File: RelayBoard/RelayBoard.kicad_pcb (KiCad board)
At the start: 2 copper layers, 49.5 x 49.5 mm, 17 parts, among them K1 CONN_3, K2 CONN_3, K3 CONN_3, Q1 2N4401, Q2 2N4401, Q3 2N4401

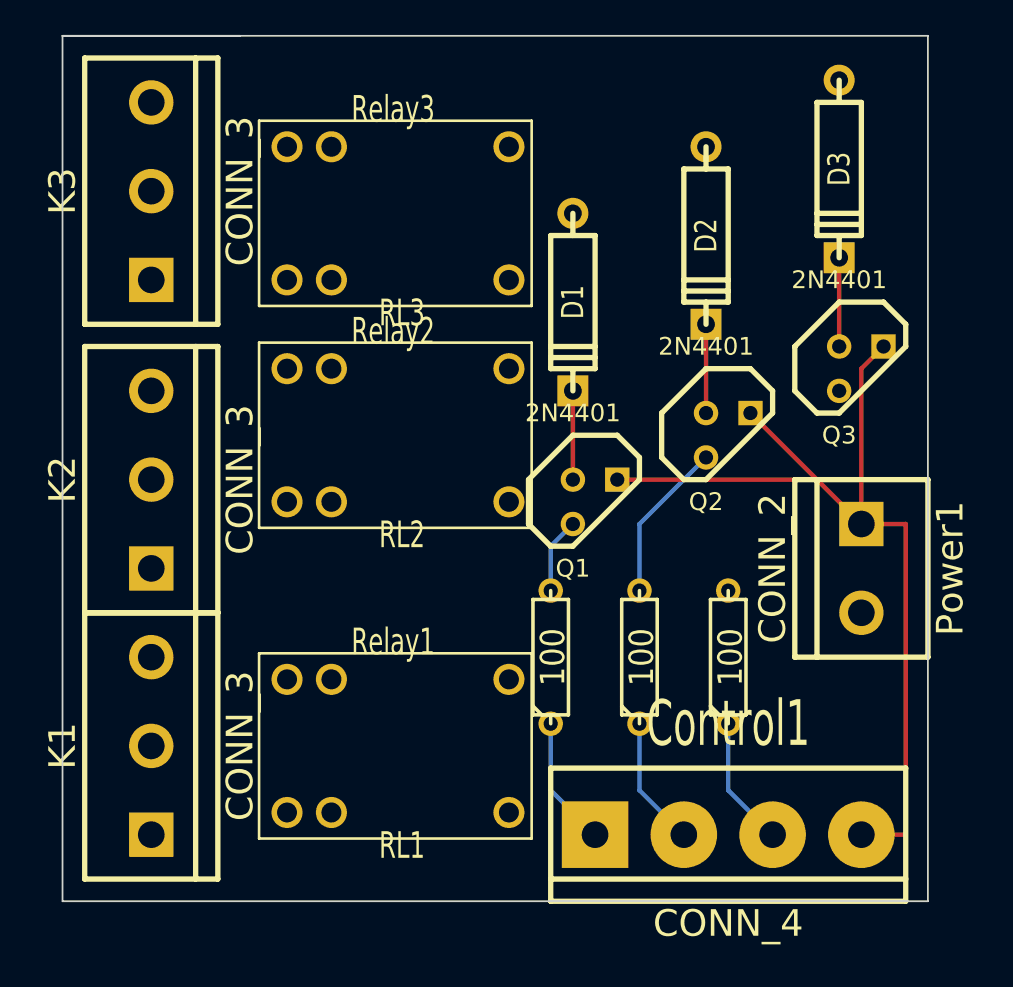
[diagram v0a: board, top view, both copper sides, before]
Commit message: Completed RelayBoard PCB Design
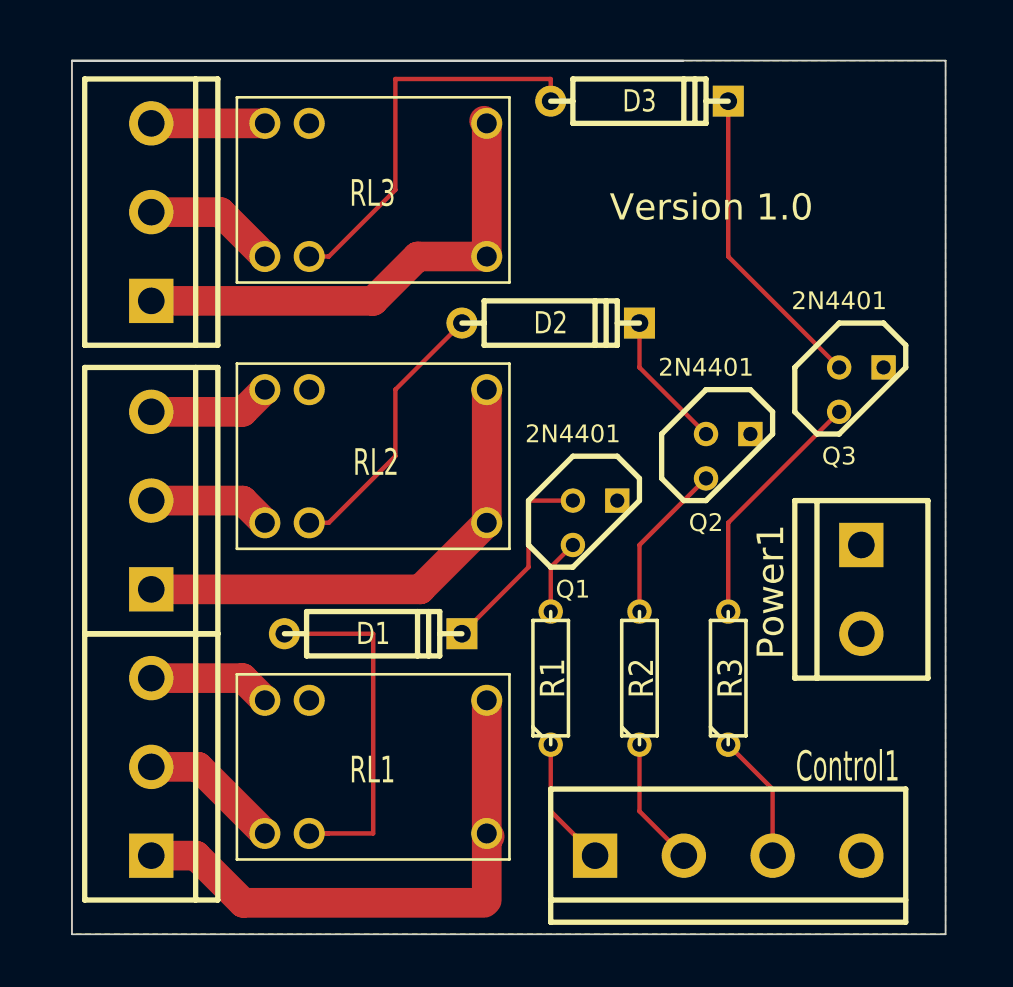
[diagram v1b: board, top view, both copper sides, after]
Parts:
- R1: value 100 -> R1
- R2: value 100 -> R2
- R3: value 100 -> R3
- moved D1 22.2 mm to (142.2, 102.8), turned to 0 degrees
- moved D3 12.1 mm to (157.5, 72.3), turned to 0 degrees
- moved D2 10.2 mm to (152.4, 85.0), turned to 0 degrees
- moved RL3 1.85 mm to (142.2, 77.4)
- moved RL1 1.75 mm to (142.2, 110.4)
- moved RL2 1.75 mm to (142.2, 92.6)
- moved Control1 1.20 mm to (162.6, 115.5)
- moved K1 1.20 mm to (129.5, 110.4)
- moved K2 1.20 mm to (129.5, 95.2)
- moved K3 1.20 mm to (129.5, 78.7)
- moved Power1 1.20 mm to (170.2, 100.3)
- moved Q1 1.20 mm to (154.9, 96.5)
- moved Q2 1.20 mm to (162.6, 92.6)
- moved Q3 1.20 mm to (170.2, 88.8)
- moved R1 1.20 mm to (152.4, 105.3)
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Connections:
- K1 pad 1: N-000005 -> N-000009
- K1 pad 2: N-000004 -> N-000007
- K1 pad 3: N-000003 -> N-000008
- K2 pad 1: N-000009 -> N-000002
- K2 pad 2: N-000007 -> N-000006
- K2 pad 3: N-000008 -> N-000001
- K3 pad 1: N-000002 -> N-000005
- K3 pad 2: N-000006 -> N-000004
- K3 pad 3: N-000001 -> N-000003
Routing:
- net GND: track 54.0 -> 0.00 mm
- net N-000009: track 0.00 -> 31.9 mm
- net N-000002: track 0.00 -> 28.4 mm
- net N-000005: track 0.00 -> 28.1 mm
- net N-0000020: track 0.00 -> 23.0 mm
- net N-0000022: track 0.00 -> 21.3 mm
- net N-0000021: track 0.00 -> 15.7 mm
- net N-0000015: track 0.00 -> 14.1 mm
- net N-0000010: track 5.08 -> 17.9 mm
- net N-000007: track 0.00 -> 8.08 mm
- net N-000004: track 0.00 -> 7.55 mm
- net N-000008: track 0.00 -> 7.03 mm
- net N-000006: track 0.00 -> 7.03 mm
- net N-000001: track 0.00 -> 7.03 mm
- net N-0000014: track 5.08 -> 11.7 mm
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- added copper zone on B.Cu, net GND
- added copper zone on F.Cu, net VCC
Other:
- board size 49.5 x 49.5 mm -> 50 x 50 mm
- net class Default: trace_width 0.254 -> 1.7
- board text added: "Version 1.0"

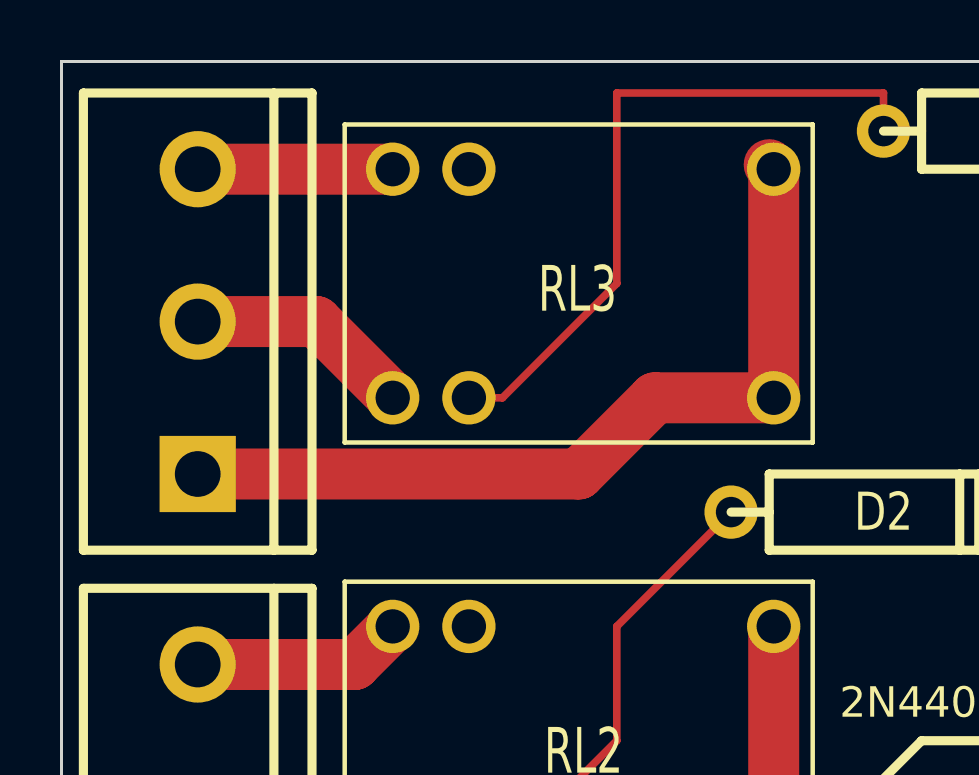
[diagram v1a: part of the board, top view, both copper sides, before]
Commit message: Completed RelayBoard PCB Design
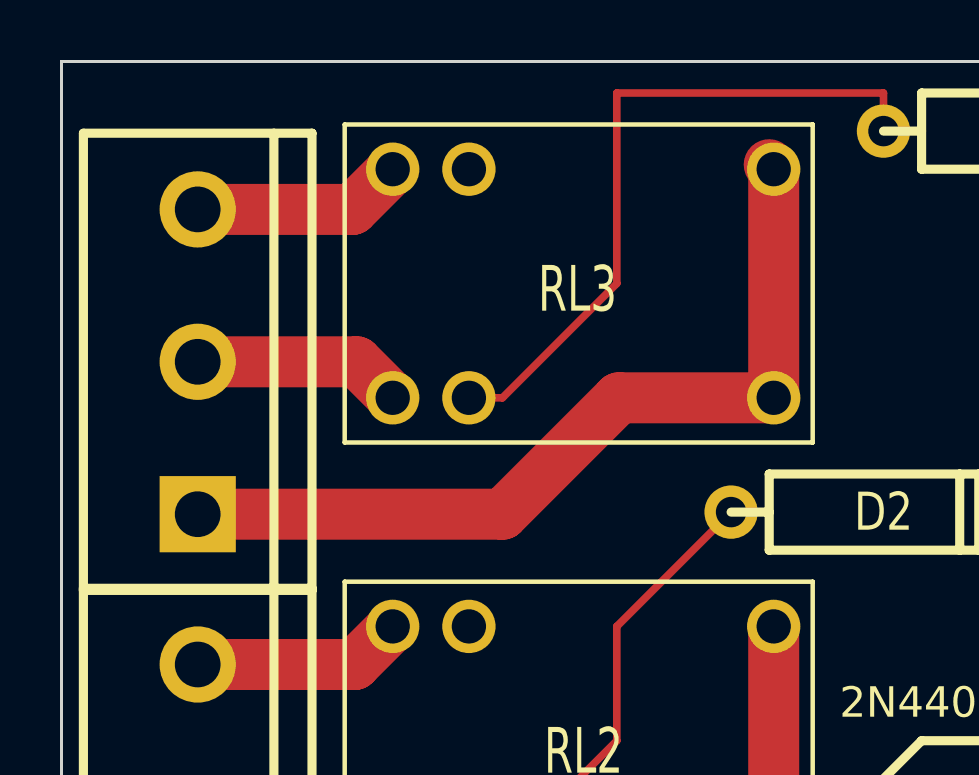
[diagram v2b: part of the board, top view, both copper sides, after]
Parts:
- moved K3 1.34 mm to (129.5, 80.0)
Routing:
- net N-000003: track 6.50 -> 7.06 mm
- net N-000004: track 7.55 -> 7.00 mm
- net N-000005: track 28.1 -> 28.6 mm
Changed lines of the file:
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@@
     (links 31)
     (no_connects 0)
-    (area 123.2916 69.9324 176.4284 121.7484)
+    (area 123.2916 69.9324 175.050001 121.7484)
     (thickness 1.6)
     (drawings 6)
-    (tracks 57)
+    (tracks 58)
     (zones 0)
     (modules 17)
@@
   )
   (module bornier3 (layer F.Cu)
-    (at 129.54 78.67 90)
+    (at 129.54 80.01 90)
     (descr "Bornier d'alimentation 3 pins")
     (tags DEV)
@@
   (segment (start 157.48 109.15) (end 157.48 112.96) (width 0.254) (layer F.Cu) (net 15))
   (segment (start 157.48 112.96) (end 160.02 115.5) (width 0.254) (layer F.Cu) (net 15))
-  (segment (start 129.54 73.59) (end 136.04 73.59) (width 1.7) (layer F.Cu) (net 16))
-  (segment (start 129.54 78.67) (end 133.5 78.67) (width 1.7) (layer F.Cu) (net 17))
-  (segment (start 133.5 78.67) (end 136.04 81.21) (width 1.7) (layer F.Cu) (net 17))
-  (segment (start 129.54 83.75) (end 142.24 83.75) (width 1.7) (layer F.Cu) (net 18))
-  (segment (start 144.78 81.21) (end 148.74 81.21) (width 1.7) (layer F.Cu) (net 18))
-  (segment (start 142.24 83.75) (end 144.78 81.21) (width 1.7) (layer F.Cu) (net 18))
+  (segment (start 129.54 74.93) (end 134.7 74.93) (width 1.7) (layer F.Cu) (net 16))
+  (segment (start 134.7 74.93) (end 136.04 73.59) (width 1.7) (layer F.Cu) (net 16))
+  (segment (start 129.54 80.01) (end 134.84 80.01) (width 1.7) (layer F.Cu) (net 17))
+  (segment (start 134.84 80.01) (end 136.04 81.21) (width 1.7) (layer F.Cu) (net 17))
+  (segment (start 129.54 85.09) (end 139.7 85.09) (width 1.7) (layer F.Cu) (net 18))
+  (segment (start 143.58 81.21) (end 148.74 81.21) (width 1.7) (layer F.Cu) (net 18))
+  (segment (start 139.7 85.09) (end 143.58 81.21) (width 1.7) (layer F.Cu) (net 18))
   (segment (start 148.74 81.21) (end 148.74 73.59) (width 1.7) (layer F.Cu) (net 18))
   (segment (start 148.74 73.59) (end 148.59 73.44) (width 1.7) (layer F.Cu) (net 18))
@@
   (segment (start 129.54 105.34) (end 134.77 105.34) (width 1.7) (layer F.Cu) (net 21))
   (segment (start 134.77 105.34) (end 136.04 106.61) (width 1.7) (layer F.Cu) (net 21))
-  (segment (start 148.74 106.61) (end 148.74 114.23) (width 1.7) (layer F.Cu) (net 22) (status C00000))
-  (segment (start 148.74 114.23) (end 148.91 114.4) (width 1.7) (layer F.Cu) (net 22) (status C00000))
-  (segment (start 148.74 114.23) (end 148.74 118.06) (width 1.7) (layer F.Cu) (net 22) (status 400000))
+  (segment (start 148.74 106.61) (end 148.74 114.23) (width 1.7) (layer F.Cu) (net 22))
+  (segment (start 148.74 114.23) (end 148.91 114.4) (width 1.7) (layer F.Cu) (net 22))
+  (segment (start 148.74 114.23) (end 148.74 118.06) (width 1.7) (layer F.Cu) (net 22))
   (segment (start 129.54 115.5) (end 132.1 115.5) (width 1.7) (layer F.Cu) (net 22))
   (segment (start 134.8 118.2) (end 148.6 118.2) (width 1.7) (layer F.Cu) (net 22))

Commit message: Fixed pin header spacing on all connectors
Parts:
- Control1: footprint bornier4 -> PinHeader4
- K1, K2, K3: footprint bornier3 -> PinHeader3
- Power1: footprint bornier2 -> PinHeader2
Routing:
- net N-000009: track 31.9 -> 36.0 mm
- net N-000003: track 7.06 -> 10.3 mm
- net N-000001: track 7.03 -> 10.2 mm
- net N-000005: track 28.6 -> 31.2 mm
- net N-000002: track 28.4 -> 30.9 mm
- net N-000007: track 8.08 -> 10.2 mm
- net N-0000019: track 7.40 -> 8.98 mm
- net N-000008: track 7.03 -> 7.72 mm
- net N-0000023: track 7.40 -> 7.93 mm
- net N-0000016: track 7.40 -> 6.88 mm

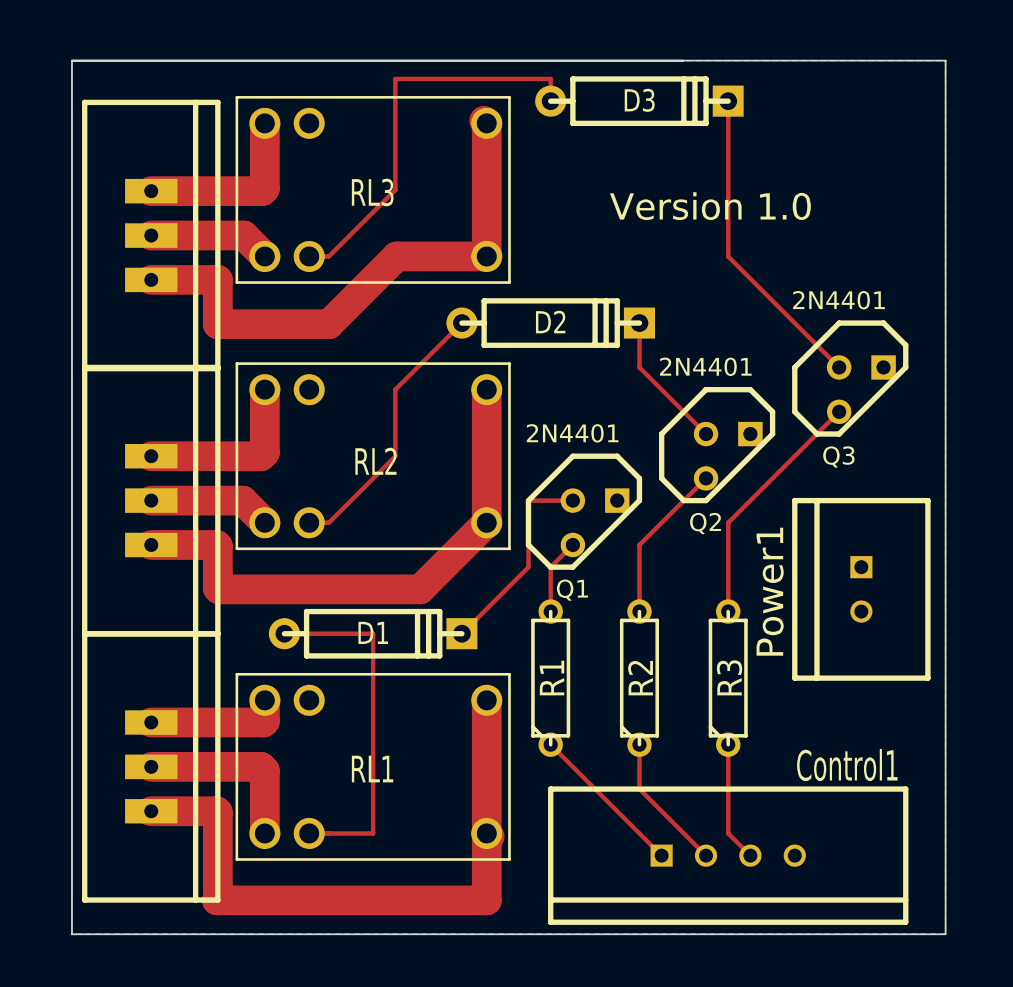
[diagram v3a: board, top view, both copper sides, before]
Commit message: Added transmitter amplifier board and the corresponding gerbers
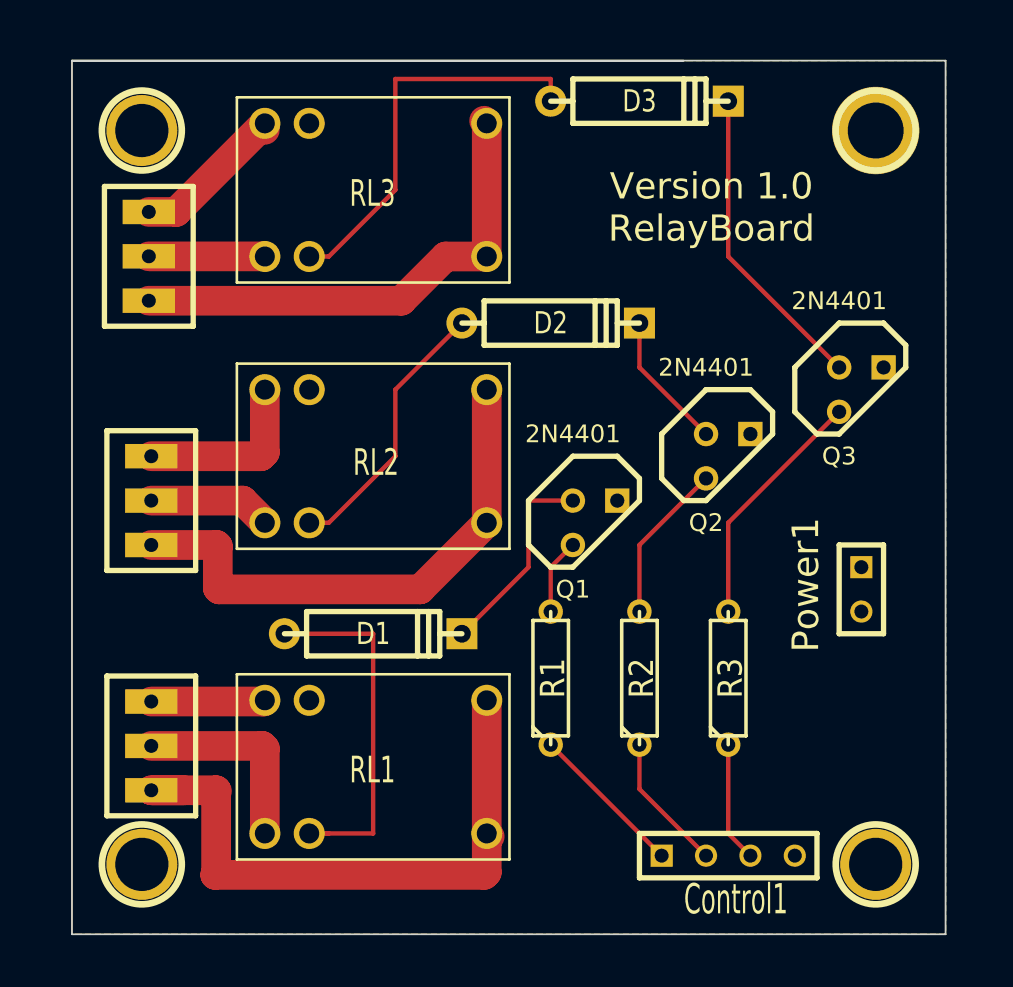
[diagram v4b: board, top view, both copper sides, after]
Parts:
- added 1PIN: P***, 1pin, F.Cu at (171.0, 74.0)
- added 1PIN: P***, 1pin, F.Cu at (171.0, 116.0)
- added 1PIN: P***, 1pin, F.Cu at (129.0, 116.0)
- added 1PIN: P***, 1pin, F.Cu at (129.0, 74.0)
- moved K1 1.20 mm to (129.5, 109.2)
- moved K3 1.20 mm to (129.4, 81.2)
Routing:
- net N-000005: track 31.2 -> 28.2 mm
- net N-000007: track 10.2 -> 11.4 mm
- net N-000008: track 7.72 -> 6.53 mm
- net N-000003: track 10.3 -> 9.11 mm
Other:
- board text added: "Version 1.0 RelayBoard"
- board text removed: "Version 1.0"
